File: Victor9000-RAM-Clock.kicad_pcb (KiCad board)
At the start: 2 copper layers, 95.2 x 87.4 mm, 21 parts, among them U1 74LS00, U2 74LS11, U3 74LS139, U4 74LS373, U5 AS6C4008-55PCN, U6 74LS245, U7 AS6C4008-55PCN, U8 DS1315-5+

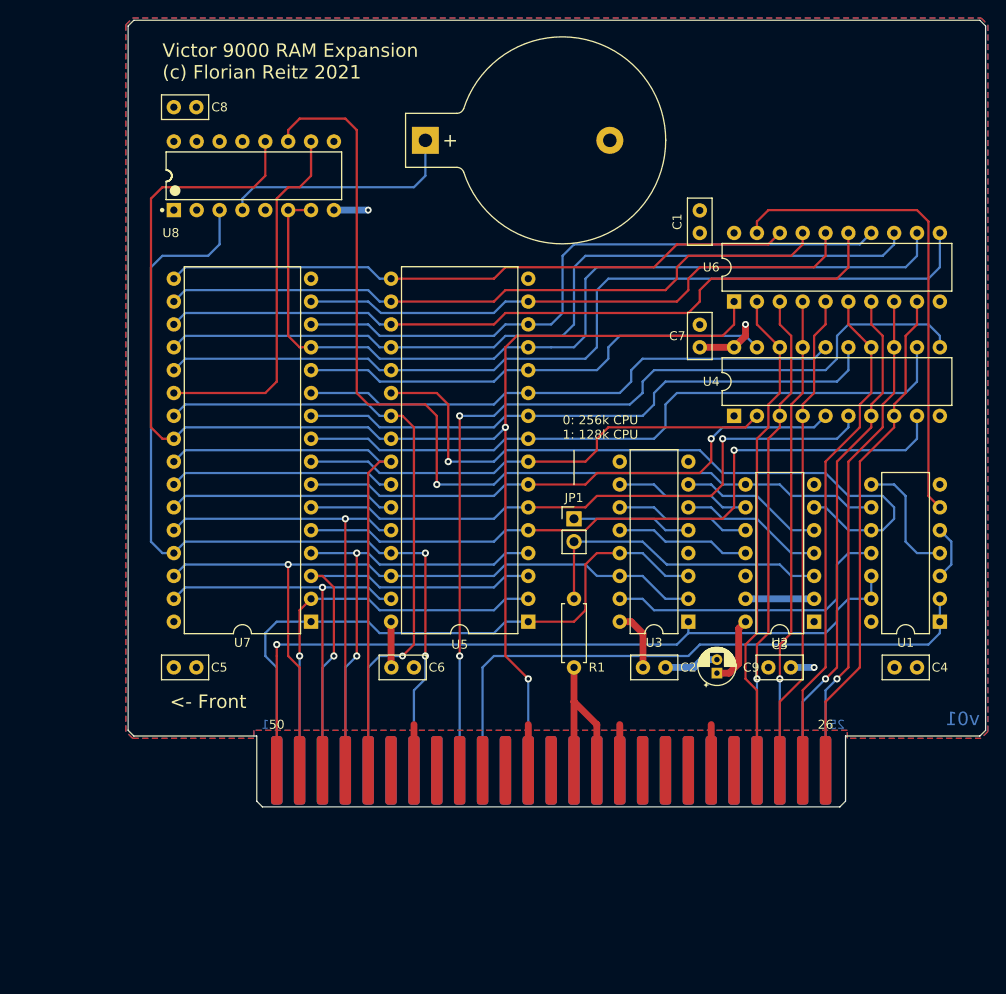
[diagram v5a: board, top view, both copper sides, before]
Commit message: Crystal added
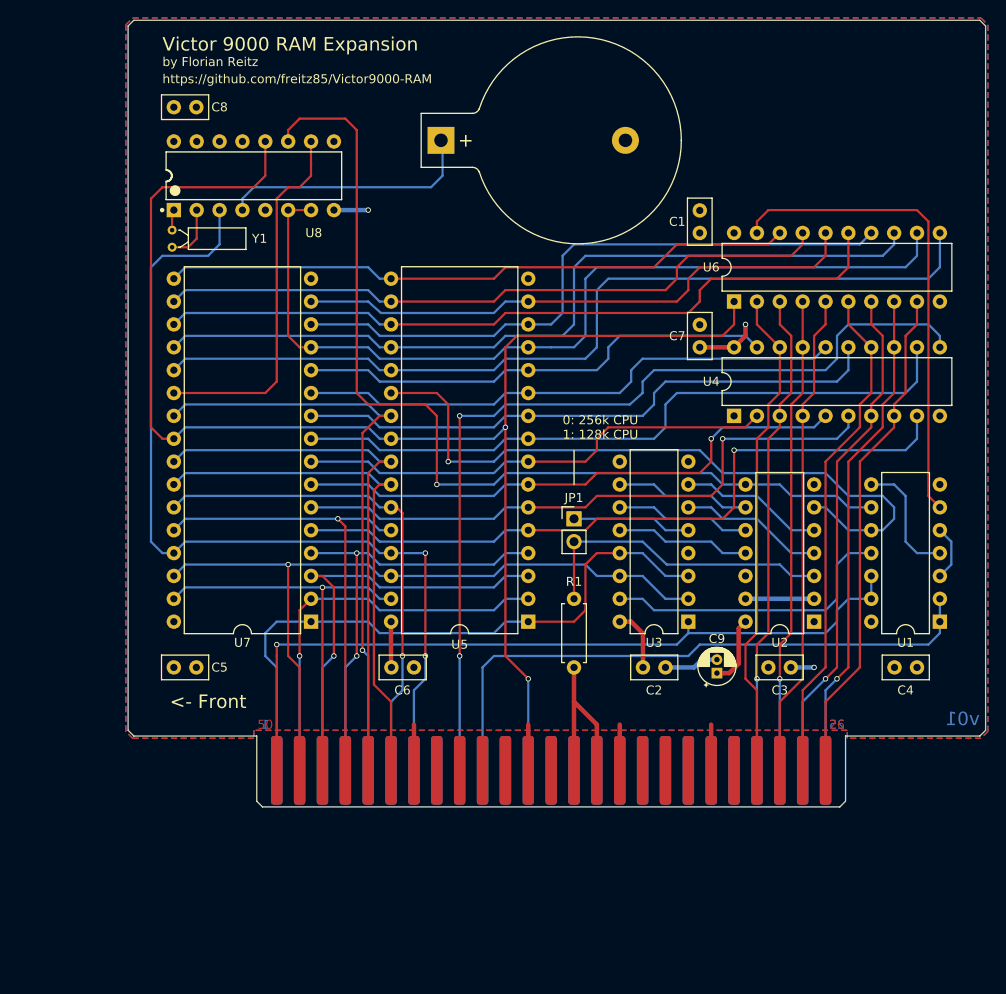
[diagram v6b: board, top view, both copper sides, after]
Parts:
- added Y1: 32.768 kHz, Crystal:Crystal_DS26_D2.0mm_L6.0mm_Horizontal, F.Cu at (98.9, 66.4)
- moved BT1 1.74 mm to (128.7, 54.5)
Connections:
- net /DT_~R renamed /DT_~{R}
- net /IO_~M renamed /IO_~{M}
- net /~EN1 renamed /~{EN1}
- net /~EN2 renamed /~{EN2}
- net /~EN2_B renamed /~{EN2_B}
- net /~SSO renamed /~{SSO}
- H1 pad 11: Net-(H1-Pad11) -> unconnected-(H1-RD-Pad11)
- H1 pad 13: /RESET -> unconnected-(H1-RESET-Pad13)
- H1 pad 14: Net-(H1-Pad14) -> unconnected-(H1-~{WR}-Pad14)
- H1 pad 15: Net-(H1-Pad15) -> unconnected-(H1-~{NMI}-Pad15)
- H1 pad 16: Net-(H1-Pad16) -> unconnected-(H1-IRQ-Pad16)
- H1 pad 17: Net-(H1-Pad17) -> unconnected-(H1-~{HOLD}-Pad17)
- H1 pad 18: Net-(H1-Pad18) -> unconnected-(H1-HLDA-Pad18)
- H1 pad 19: Net-(H1-Pad19) -> unconnected-(H1-CSEN-Pad19)
- H1 pad 20: Net-(H1-Pad20) -> unconnected-(H1-PHASE2-Pad20)
- H1 pad 21: Net-(H1-Pad21) -> unconnected-(H1-XACK-Pad21)
- H1 pad 30: Net-(H1-Pad30) -> unconnected-(H1-~{EXTIO}-Pad30)
- H1 pad 32: Net-(H1-Pad32) -> unconnected-(H1--12V-Pad32)
- H1 pad 33: Net-(H1-Pad33) -> unconnected-(H1-~{DLATCH}-Pad33)
- H1 pad 34: Net-(H1-Pad34) -> unconnected-(H1-+12V-Pad34)
- H1 pad 38: Net-(H1-Pad38) -> unconnected-(H1-CLK5-Pad38)
- H1 pad 40: Net-(H1-Pad40) -> unconnected-(H1-CLK15B-Pad40)
- H1 pad 41: Net-(H1-Pad41) -> unconnected-(H1-READY-Pad41)
- H1 pad 42: Net-(H1-Pad42) -> unconnected-(H1-IR5-Pad42)
- H1 pad 43: Net-(H1-Pad43) -> unconnected-(H1-IR4-Pad43)
- H1 pad 45: /A09 -> /A9
- H1 pad 6: /A08 -> /A8
- H1 pad 8: Net-(H1-Pad8) -> unconnected-(H1-~{DEN}-Pad8)
- U2 pad 12: Net-(U2-Pad12) -> unconnected-(U2-Pad12)
- U3 pad 4: Net-(U3-Pad4) -> unconnected-(U3A-O0-Pad4)
- U3 pad 9: Net-(U3-Pad9) -> unconnected-(U3B-O3-Pad9)
- U8 pad 13: Net-(U8-Pad13) -> unconnected-(U8-~{RST}-Pad13)
- U8 pad 15: Net-(U8-Pad15) -> unconnected-(U8-VCCO-Pad15)
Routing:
- net /A9: track 25.2 -> 59.3 mm
- net /A8: track 25.2 -> 55.8 mm, vias 0 -> 1
- net Net-(U8-X2): track 0.00 -> 6.30 mm
- net /A10: track 69.9 -> 66.9 mm
- net Net-(U8-X1): track 0.00 -> 2.30 mm
- net Net-(BT1-+): track 26.6 -> 28.5 mm
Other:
- net class Default removed
- board text added: "Victor 9000 RAM Expansion"
- board text added: "by Florian Reitz"
- board text added: "https://github.com/freitz85/Victor9000-RAM"
- board text removed: "Victor 9000 RAM Expansion (c) Florian Reitz 2021"

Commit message: Read and write access corrected
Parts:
- C9: footprint Capacitor_THT:CP_Radial_D4.0mm_P1.50mm -> Capacitor_THT:CP_Radial_D6.3mm_P2.50mm
- moved C9 0.64 mm to (159.4, 113.0), turned to -90 degrees
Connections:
- H1 pad 11: unconnected-(H1-RD-Pad11) -> /~{RD}
- H1 pad 12: /DT_~{R} -> unconnected-(H1-DT/~{R}-Pad12)
- H1 pad 14: unconnected-(H1-~{WR}-Pad14) -> /~{WR}
- H1 pad 7: /~{SSO} -> unconnected-(H1-~{SSO}-Pad7)
- U5 pad 24: /DT_~{R} -> /~{RD}
- U5 pad 29: /~{SSO} -> /~{WR}
- U6 pad 1: /DT_~{R} -> /~{RD}
- U7 pad 24: /DT_~{R} -> /~{RD}
- U7 pad 29: /~{SSO} -> /~{WR}
- U8 pad 12: /DT_~{R} -> /~{RD}
- U8 pad 3: /~{SSO} -> /~{WR}
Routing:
- net /DT_~{R}: track 161.5 -> 0.00 mm, vias 2 -> 0
- net /~{RD}: track 0.00 -> 160.4 mm, vias 0 -> 2
- net /~{WR}: track 0.00 -> 114.2 mm, vias 0 -> 2
- net /~{SSO}: track 99.7 -> 0.00 mm, vias 2 -> 0
- net GND: track 40.4 -> 34.3 mm
- net +5V: track 47.7 -> 45.6 mm
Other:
- board text added: "v02"
- board text removed: "v01"
